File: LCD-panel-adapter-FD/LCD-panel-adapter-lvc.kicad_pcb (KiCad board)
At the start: 2 copper layers, 40.6 x 48.3 mm, 13 parts, among them J101 HEADER_18, M101 LOGO_OSHW, P101 CONN_4X2, P102 CONN_5X2, P103 CONN_5X2, U101 74HC07A

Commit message: LCD-Panel-adapter: routing, gerbers
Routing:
- net GND: track 99.8 -> 113.8 mm
- net /LCD_D6_5V: track 25.2 -> 35.4 mm
- net /LCD_D5_5V: track 34.8 -> 28.0 mm
- net /SD_DO: track 44.4 -> 50.4 mm
- net /ENC2: track 42.5 -> 36.7 mm
- net /IOREF: track 34.7 -> 40.3 mm
- net /ENC_SW: track 25.4 -> 30.8 mm
- net /BEEP: track 25.6 -> 30.7 mm, vias 1 -> 0
- net +5V: track 53.2 -> 55.2 mm
- net /SD_DI: track 38.4 -> 36.7 mm
- net /LCD_E: track 14.2 -> 12.7 mm
- net /LCD_RS: track 19.7 -> 18.2 mm
- net /LCD_E_5V: track 43.4 -> 44.2 mm
- net /SD_DETECT: track 38.5 -> 39.3 mm
- net /LCD_D4: track 7.04 -> 6.37 mm
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
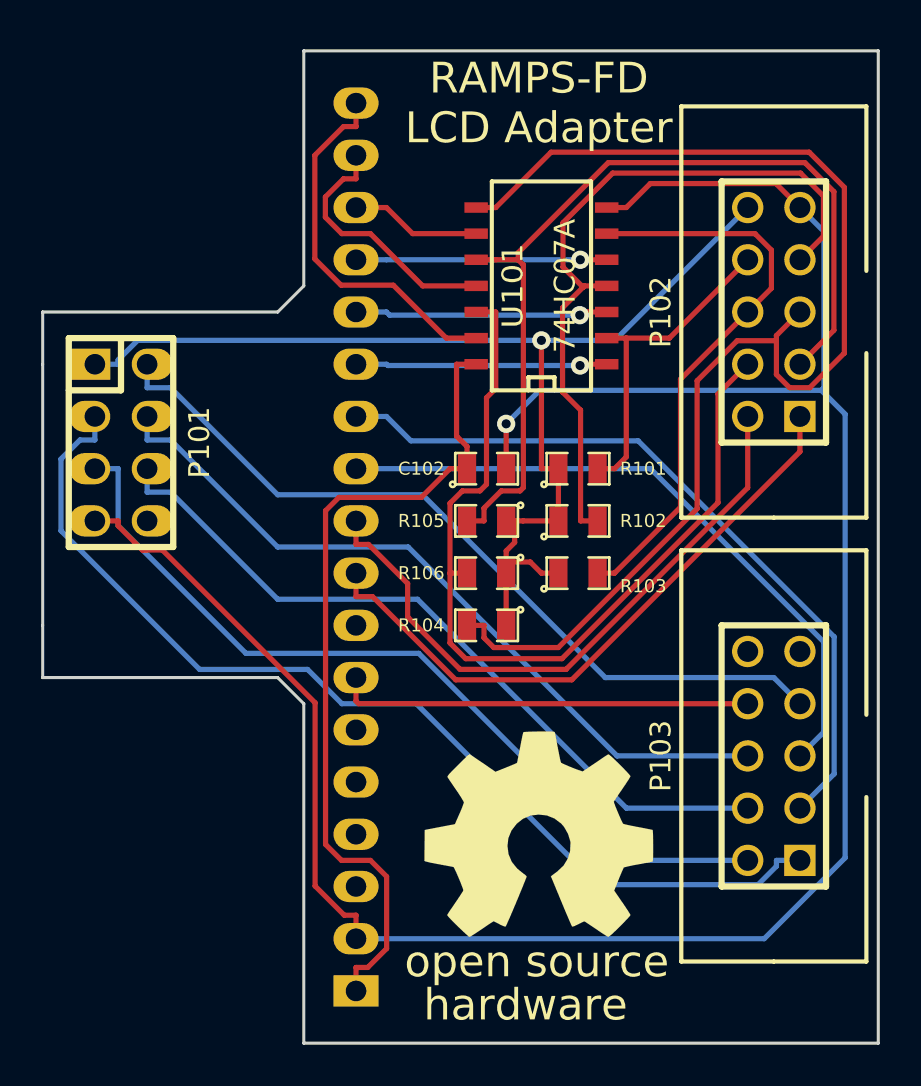
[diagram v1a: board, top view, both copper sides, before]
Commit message: LCD-Panel-adapter-FD: update and add gerbers
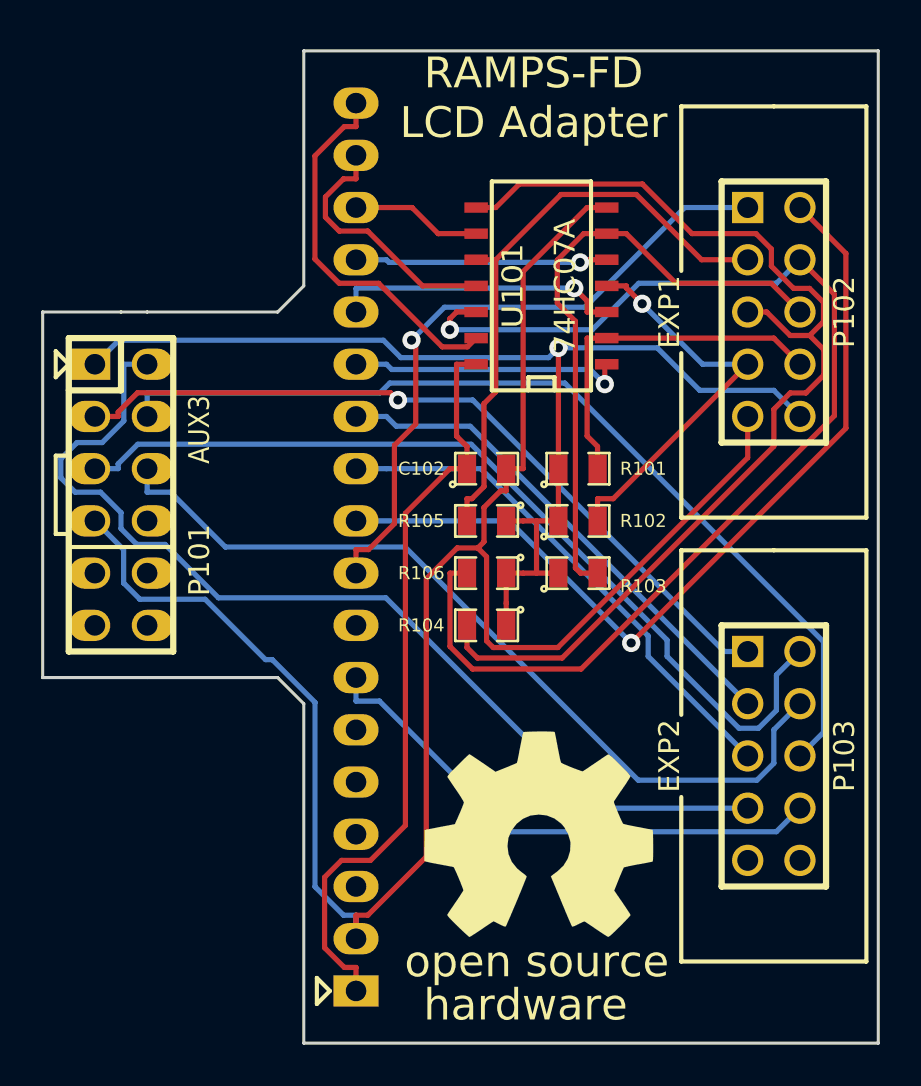
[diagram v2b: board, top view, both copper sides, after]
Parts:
- J101: value HEADER_18 -> AUX4
- P101: value CONN_4X2 -> AUX3; footprint pin_strip_4x2 -> pin_strip_6x2
- P102: value CONN_5X2 -> EXP1
- P103: value CONN_5X2 -> EXP2
- moved P101 2.54 mm to (138.4, 94.0)
- turned P102 to 270 degrees
- turned P103 to 270 degrees
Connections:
- net /BEEP renamed BEEP
- net /ENC1 renamed ENC1
- net /ENC2 renamed ENC2
- net /ENC_SW renamed ENC_SW
- net /LCD_D4 renamed LCD_D4
- net /LCD_D5 renamed LCD_D5
- net /LCD_D6 renamed LCD_D6
- net /LCD_D7 renamed LCD_D7
- net /LCD_E renamed LCD_E
- net /LCD_RS renamed LCD_RS
- net /RESET renamed RESET
- net /SD_CLK renamed SD_CLK
- net /SD_CS renamed SD_CS
- net /SD_DETECT renamed SD_DETECT
- net /SD_DI renamed SD_DI
- net /SD_DO renamed SD_DO
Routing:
- net GND: track 113.8 -> 94.1 mm, vias 1 -> 0
- net /LCD_D6_5V: track 35.4 -> 19.6 mm, vias 0 -> 1
- net /LCD_E_5V: track 44.2 -> 29.3 mm
- net /LCD_RS_5V: track 43.1 -> 57.3 mm, vias 0 -> 1
- net SD_DO: track 50.4 -> 37.6 mm, vias 0 -> 1
- net ENC2: track 36.7 -> 24.8 mm
- net ENC_SW: track 30.8 -> 42.3 mm, vias 0 -> 1
- net SD_DETECT: track 39.3 -> 49.2 mm
- net SD_DI: track 36.7 -> 45.5 mm
- net /LCD_D4_5V: track 61.3 -> 53.2 mm
- net ENC1: track 32.3 -> 25.4 mm
- net RESET: track 20.2 -> 25.8 mm
- net SD_CS: track 36.7 -> 41.2 mm
- net /IOREF: track 40.3 -> 36.8 mm
- net SD_CLK: track 41.3 -> 43.7 mm
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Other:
- outline, holes or cut-outs redrawn
